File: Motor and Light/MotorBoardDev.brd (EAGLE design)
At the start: 98.5 x 86 mm, 92 parts, among them IC1 74HC04D, J1 Under Glow, J2 Safety Light, J3 12V, J4 24V, Q1 BC846ASMD, Q2 220mA/50V/3.5Ω, Q7 220mA/50V/3.5Ω, Q8 220mA/50V/3.5Ω, Q9 220mA/50V/3.5Ω, T12 TIP41A, T13 TIP41A, T14 TIP41A, T15 TIP41A, T16 TIP41A, T18 TIP41A, T2 TIP41A, U1 TIP41C, U2 9DoF IMU, U3 TIP41C, U4 TIP41C, X1 C-GRID-05-15-91, X2 C-GRID-05-15-91, X4 C-GRID-02-70553, X5 SI-50170, X7 2510-, X8 2510-

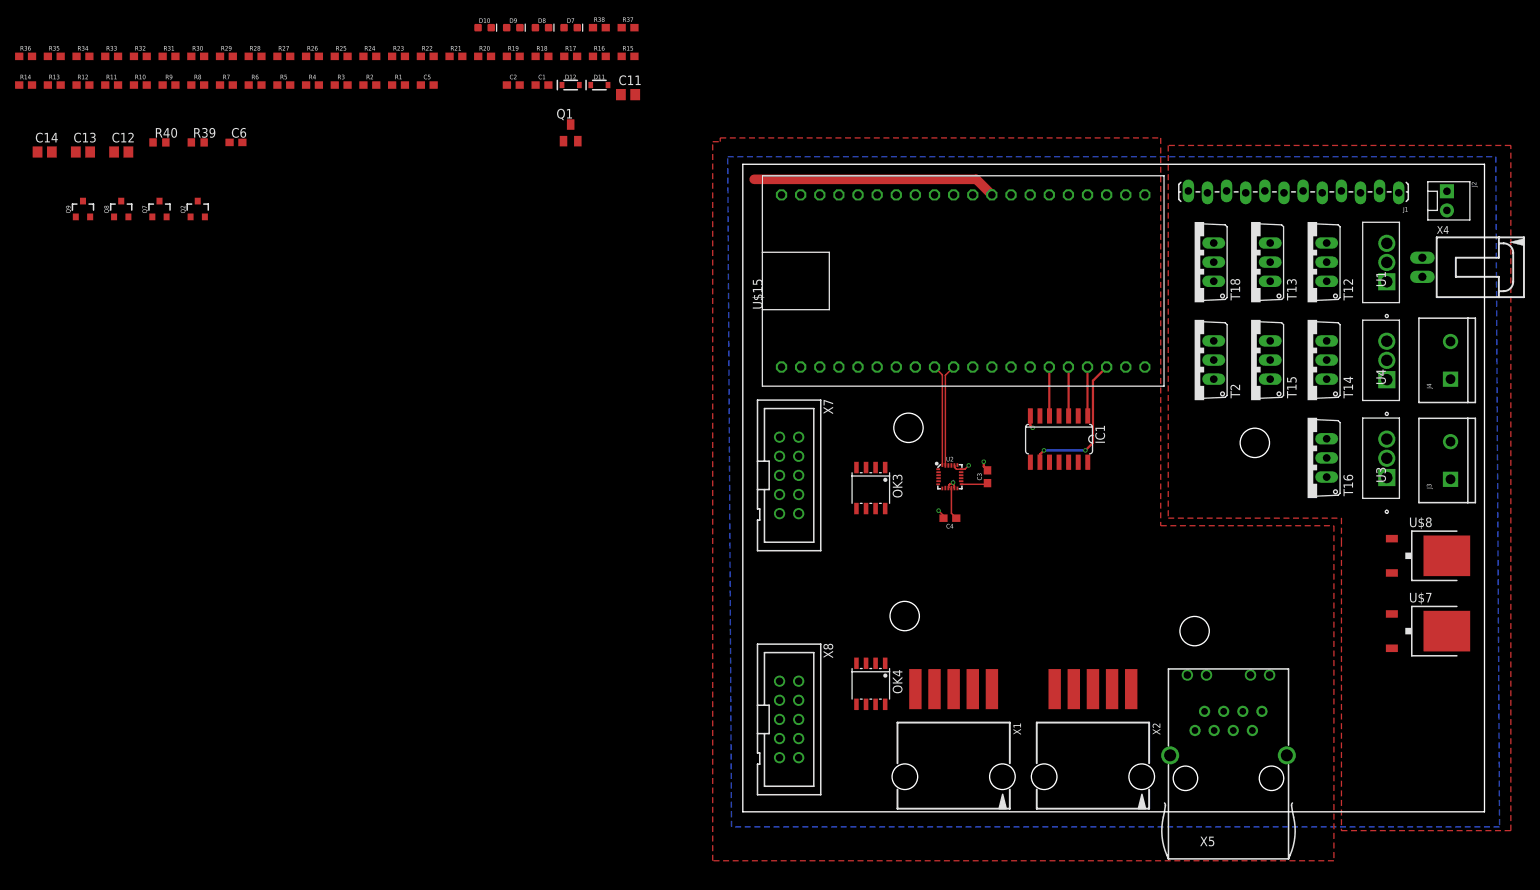
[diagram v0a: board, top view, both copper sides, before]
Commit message: Primary Layout Complete
Layout Complete, Sorting through Libraries
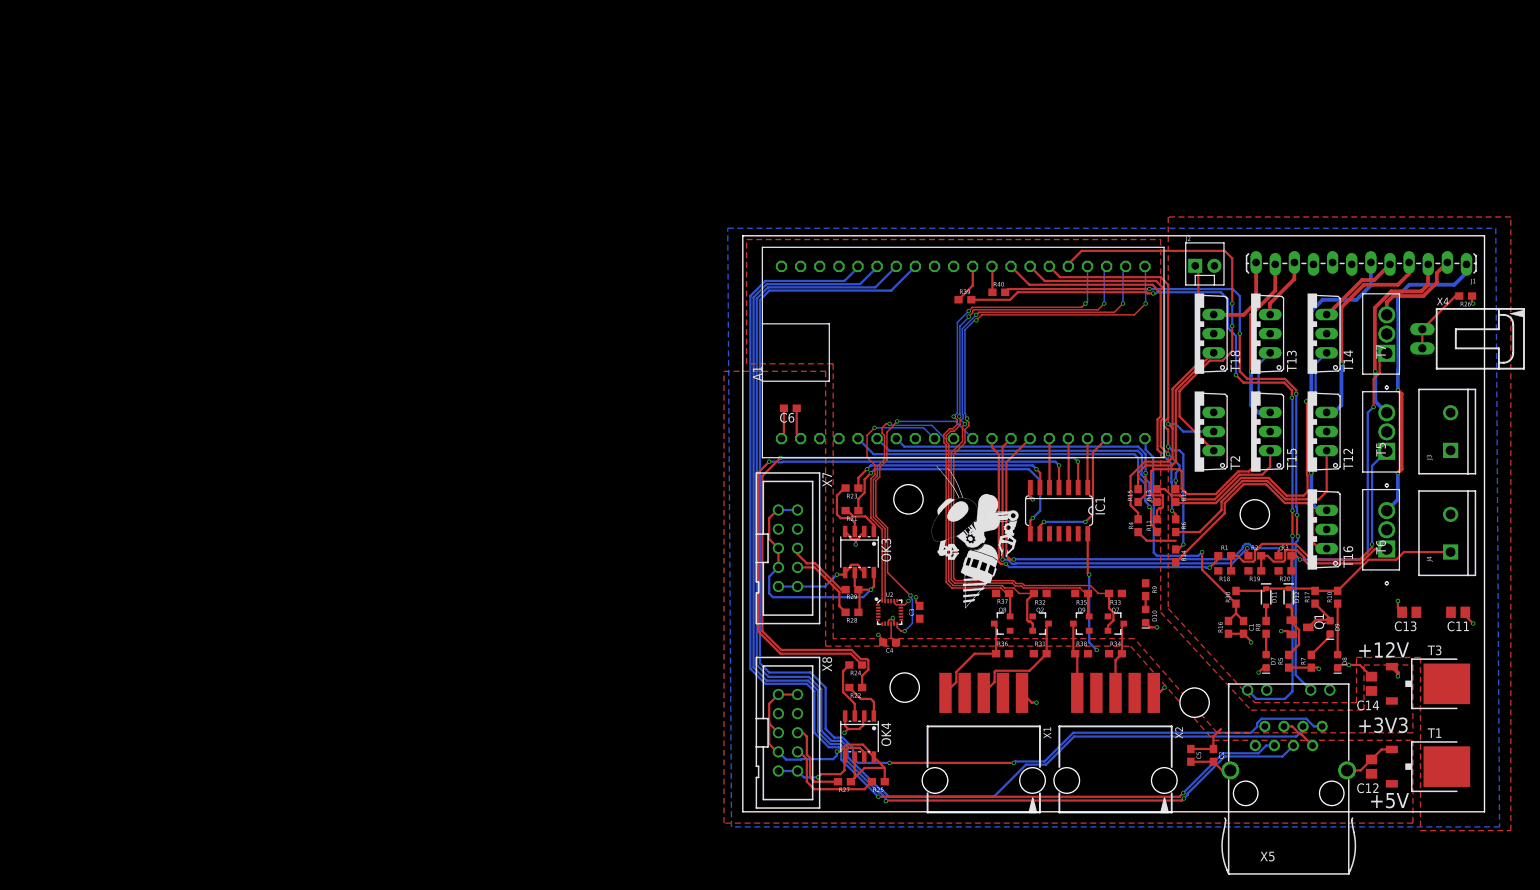
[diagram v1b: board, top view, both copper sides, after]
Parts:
- removed U$15: MBED1768, SparkFun-Boards:DIL40_0.9
- removed U$7: NCP1117DT50GOS-ND, IGVC-Regulators:TO252
- removed U$8: NCP1117DT33GOS-ND, IGVC-Regulators:TO252
- removed U1, U3, U4: TIP41C, DigiKey:TO-220
- added A1: MBED1768, MotorBoardDev:SPARKFUN-BOARDS_DIL40_0.9
- added T1: NCP1117DT50GOS-ND, IGVC-Regulators:TO252
- added T3: NCP1117DT33GOS-ND, IGVC-Regulators:TO252
- added T5, T6, T7: TIP41C, DigiKey:TO-220
- added U$5: (no value), RoboJackets-Aesthetics:ROBOBUZZ_1.0X
- R39, R40: value 150 -> 500; device rcl:R0603 -> SparkFun-Resistors:0603
- moved C14 189.8 mm to (83.5, 17.0), turned to 90 degrees
- moved C13 186.4 mm to (88.5, 26.5), turned to 180 degrees
- moved C12 185.0 mm to (83.5, 6.00), turned to 90 degrees
- moved R10 172.9 mm to (79.0, 28.5), turned to 90 degrees
- moved R14 165.0 mm to (57.5, 34.0), turned to 270 degrees
- moved R7 163.1 mm to (75.5, 20.0), turned to 90 degrees
- moved R8 159.1 mm to (69.5, 24.5), turned to 90 degrees
- moved R34 158.4 mm to (49.5, 21.0), turned to 180 degrees
- moved R26 156.4 mm to (96.0, 68.5), turned to 180 degrees
- moved R13 156.3 mm to (55.0, 42.0), turned to 90 degrees
- moved R30 155.5 mm to (65.5, 28.5), turned to 90 degrees
- moved R12 155.0 mm to (57.5, 42.0), turned to 270 degrees
- moved R35 154.0 mm to (45.0, 29.0), turned to 180 degrees
- moved R5 153.8 mm to (72.5, 20.0), turned to 90 degrees
- moved R36 152.1 mm to (34.5, 21.0)
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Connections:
- net +12V: now also T1.3, T3.3, T5.2, T6.2, T7.2; no longer U$7.3, U$8.3, U1.2, U3.2, U4.2
- net +3V3: now also A1.40, T3.2; no longer U$15.40, U$8.2
- net +5V: now also A1.2, T1.2; no longer U$15.2, U$7.2
- net 1S1: now also A1.28; no longer U$15.28
- net 1S2: now also A1.27; no longer U$15.27
- net 1S3: now also A1.26; no longer U$15.26
- net 2S1: now also A1.5; no longer U$15.5
- net 2S2: now also A1.6; no longer U$15.6
- net 2S3: now also A1.7; no longer U$15.7
- net BATTIN: now also A1.20; no longer U$15.20
- net BLUE: now also A1.13; no longer U$15.12
- net BLUE_OUT: now also T6.3; no longer U3.3
- net GND: now also A1.1, T1.1, T3.1; no longer U$15.1, U$7.1, U$8.1
- net GREEN: now also A1.14; no longer U$15.13
- net GREEN_OUT: now also T7.3; no longer U4.3
- net GYRO_INT: now also A1.11; no longer U$15.14
- net LDIR: now also A1.17; no longer U$15.17
- net LEA3: now also A1.23; no longer U$15.24
- net LEB3: now also A1.24; no longer U$15.23
- net LSPEED: now also A1.18; no longer U$15.18
- net N$10: now also T7.1; no longer U4.1
- net N$3: now also T5.1; no longer U1.1
- net N$37: now also A1.30; no longer U$15.30
- net N$38: now also A1.29; no longer U$15.29
- net N$4: now also T6.1; no longer U3.1
- net RD+: now also A1.35; no longer U$15.35
- net RD-: now also A1.36; no longer U$15.36
- net RDIR: now also A1.15; no longer U$15.15
- net REA3: now also A1.21; no longer U$15.22
- net REB3: now also A1.22; no longer U$15.21
- net RED: now also A1.12; no longer U$15.11
- net RED_OUT: now also T5.3; no longer U1.3
- net RSPEED: now also A1.16; no longer U$15.16
- net SAFETY_LIGHT: now also A1.25; no longer U$15.25
- net SCL: now also A1.10; no longer U$15.10
- net SDA: now also A1.9; no longer U$15.9
- net TD+: now also A1.33; no longer U$15.33
- net TD-: now also A1.34; no longer U$15.34
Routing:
- net TD+: track 0.00 -> 158.0 mm, vias 0 -> 2
- net TD-: track 0.00 -> 156.9 mm
- net RD+: track 0.00 -> 153.9 mm, vias 0 -> 2
- net RD-: track 0.00 -> 149.0 mm, vias 0 -> 2
- net ETH_LED1: track 0.00 -> 100.7 mm, vias 0 -> 5
- net REA3: track 0.00 -> 91.6 mm, vias 0 -> 3
- net ETH_LED2: track 0.00 -> 91.1 mm, vias 0 -> 5
- net !RSPEED!: track 0.00 -> 86.8 mm, vias 0 -> 2
- net REB3: track 0.00 -> 84.4 mm, vias 0 -> 3
- net !RDIR!: track 0.00 -> 80.5 mm, vias 0 -> 2
- net LEA3: track 0.00 -> 78.6 mm, vias 0 -> 3
- net LEB3: track 0.00 -> 71.2 mm, vias 0 -> 3
- net GREEN: track 0.00 -> 56.0 mm, vias 0 -> 2
- net GND: track 8.93 -> 64.5 mm, vias 5 -> 19
- net SAFETY_LIGHT: track 0.00 -> 54.5 mm, vias 0 -> 2
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- added copper zone on layer 1, net +5V
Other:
- board size 98.5 x 86 mm -> 98.5 x 76.5 mm
- board text added: "+12V"
- board text added: "+3V3"
- board text added: "+5V"

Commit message: Updated Schematics Commit
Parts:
- removed D10: WHITE, SparkFun-LED:LED-0603
- removed D11, D12: 3.3V, SparkFun-DiscreteSemi:SOD-323
- removed D7: RED, SparkFun-LED:LED-0603
- removed D8: BLUE, SparkFun-LED:LED-0603
- removed D9: GREEN, SparkFun-LED:LED-0603
- removed IC1: 74HC04D, 74xx-eu:SO14
- removed R18, R19, R20: 200, SparkFun-Resistors:0603
- removed R26, R30: 2700, SparkFun-Resistors:0603
- removed T12, T13, T14, T15, T16, T18: TIP41A, transistor:TO220V
- removed T5, T6, T7: TIP41C, DigiKey:TO-220
- added C7, C8: 10uF, rcl:C0805
- added D1, D2: GREEN, SparkFun-LED:LED-0603
- added D3: WHITE, SparkFun-LED:LED-0603
- added D4: BLUE, SparkFun-LED:LED-0603
- added FQP30N06L, Q15, Q16: TIP41C, transistor-power:TO220AV
- added Q10, Q11, Q3, Q4, Q5, Q6: TIP42C, transistor-power:TO220AV
- added X3: MINI-USB_SHIELD5P4-32005-400, con-cypressindustries:32005-400
- C11, C12, C13, C14: value (none) -> 10uF
- Q1: value BC846ASMD -> TIP42C; device transistor-npn:SOT23 -> transistor-power:TO220AV
- R10: value 2700 -> 200
- R16: value 536 -> 200
- R7: value 200 -> 50
- R8: value 2700 -> 1800
- R9: value 2700 -> 1000
- U$5: device RoboJackets-Aesthetics:ROBOBUZZ_1.0X -> RoboJackets-Aesthetics:ROBOBUZZ_1.2X
- moved R17 348.9 mm to (0.00, -312.0), turned to 0 degrees
- moved C1 324.4 mm to (0.00, -293.0), turned to 0 degrees
- moved R10 324.3 mm to (0.00, -286.0), turned to 0 degrees
- moved R16 320.6 mm to (0.00, -289.5), turned to 0 degrees
- moved R9 316.6 mm to (0.00, -282.5), turned to 0 degrees
- moved R8 311.4 mm to (0.00, -279.0), turned to 0 degrees
- moved R7 298.2 mm to (0.00, -268.5), turned to 0 degrees
- moved R5 294.1 mm to (0.00, -265.0), turned to 0 degrees
- moved Q1 107.5 mm to (7.50, -60.0), turned to 0 degrees
- moved T2 95.3 mm to (7.50, -29.0), turned to 0 degrees
- moved U$5 4.27 mm to (28.0, 23.0)
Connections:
- removed net !LDIR!: IC1.6, R23.1
- removed net !LSPEED!: IC1.8, R21.1
- removed net !RDIR!: IC1.4, R24.1
- removed net !RSPEED!: IC1.2, R22.1
- removed net N$24: D9.A, Q1.3, R17.1
- removed net N$33: D9.C, R7.2
- removed net N$34: D8.A, R10.1
- removed net N$35: D10.A, R9.1
- removed net N$7: D7.A, R8.1
- new net D+: A1.31, X3.3
- new net D-: A1.32, X3.2
- new net ID: X3.4
- new net INDICATOR_LED: A1.8
- new net N$12: D4.A, R9.1
- new net N$5: D1.A, R5.1
- new net N$8: Q11.E, R17.1, X4.1
- net +12V: now also C7.1, FQP30N06L.C, Q15.C, Q16.C, R17.2, R9.2; no longer R18.2, R19.2, R20.2, T5.2, T6.2, T7.2
- net +24V: now also C8.1, R8.2; no longer D11.C, D12.C, R17.2, R30.2
- net +3V3: now also R7.2; no longer R9.2
- net +5V: now also A1.39, R5.2, X3.1; no longer IC1.14
- net 1S1: now also A1.16; no longer A1.28
- net 1S1O: now also J1.7, Q1.E; no longer J1.4, T12.3
- net 1S2: now also A1.17; no longer A1.27
- net 1S2O: now also J1.6, Q4.E; no longer J1.5, T14.3
- net 1S3: now also A1.18; no longer A1.26
- net 1S3O: now also J1.5, Q6.E; no longer J1.6, T16.3
- net 2S1O: now also Q3.E; no longer T13.3
- net 2S2O: now also Q5.E; no longer T15.3
- net 2S3O: now also Q10.E; no longer T18.3
- net BATTIN: now also R10.1; no longer R30.1
- net BLUE: now also A1.21; no longer A1.13
- net BLUE_OUT: now also Q15.E; no longer T6.3
- net ESTOP: now also A1.24, Q11.B; no longer R26.2, X4.1, X4.2
- net GND: now also C7.2, C8.2, D1.C, D2.C, D3.C, D4.C, J1.4, J1.8, J1.9, J2.2, Q1.C, Q10.C, Q11.C, Q3.C, Q4.C, Q5.C, Q6.C, T2.2, X3.5, X4.2; no longer D10.C, D7.C, D8.C, IC1.7, Q1.2, R26.1, R5.1, R7.1, T12.2, T13.2, T14.2, T15.2, T16.2, T18.2, T2.3
- net GREEN: now also A1.22; no longer A1.14
- net GREEN_OUT: now also Q16.E; no longer T7.3
- net L+12V: now also R28.2; no longer OK3.6, OK3.8, R28.1
- net LALI: now also OK3.8
- net LBLI: now also OK3.6, R28.1; no longer R28.2
- net LDIR: now also A1.26, R23.1; no longer A1.17, IC1.1
- net LEA3: now also A1.13; no longer A1.23
- net LEB3: now also A1.12; no longer A1.24
- net LSPEED: now also A1.25, R21.1; no longer A1.18, IC1.9
- net N$1: now also T2.3; no longer T2.2
- net N$10: now also Q16.B; no longer R20.1, T7.1
- net N$11: now also Q6.B; no longer T16.1
- net N$13: now also Q4.B; no longer T14.1
- net N$14: now also Q1.B; no longer T12.1
- net N$15: now also Q3.B; no longer T13.1
- net N$16: now also Q5.B; no longer T15.1
- net N$28: now also Q10.B; no longer T18.1
- net N$3: now also FQP30N06L.B; no longer R18.1, T5.1
- net N$4: now also Q15.B; no longer R19.1, T6.1
- net N$6: now also D2.A, R7.1; no longer D11.A, R8.2
- net N$9: now also D3.A, R8.1; no longer D12.A, Q1.1, R5.2
- net R+12V: now also R25.2, R27.2; no longer OK4.6, OK4.8, R25.1, R27.1
- net RALI: now also OK4.8, R27.1; no longer R27.2
- net RBLI: now also OK4.6, R25.1; no longer R25.2
- net RDIR: now also A1.28, R24.1; no longer A1.15, IC1.5
- net REA3: now also A1.15; no longer A1.21
- net REB3: now also A1.14; no longer A1.22
- net RED: now also A1.23; no longer A1.12
- net RED_OUT: now also FQP30N06L.E; no longer T5.3
- net RSPEED: now also A1.27, R22.1; no longer A1.16, IC1.3
- net SAFETY_LIGHT: now also A1.19; no longer A1.25
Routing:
- net !RSPEED!: track 86.8 -> 0.00 mm, vias 2 -> 0
- net !RDIR!: track 80.5 -> 0.00 mm, vias 2 -> 0
- net RSPEED: track 6.51 -> 83.4 mm, vias 0 -> 2
- net RDIR: track 6.55 -> 77.6 mm, vias 0 -> 2
- net SAFETY_LIGHT: track 54.5 -> 0.00 mm, vias 2 -> 0
- net !LSPEED!: track 36.6 -> 0.00 mm, vias 2 -> 0
- net +24V: track 30.9 -> 0.00 mm
- net 1S3O: track 40.3 -> 11.1 mm, vias 2 -> 0
- net 1S2O: track 11.2 -> 40.3 mm, vias 0 -> 2
- net !LDIR!: track 28.5 -> 0.00 mm, vias 2 -> 0
- net 1S1O: track 27.7 -> 0.00 mm, vias 1 -> 0
- net LDIR: track 6.51 -> 28.5 mm, vias 0 -> 2
- net +5V: track 21.2 -> 5.25 mm, vias 2 -> 0
- net LSPEED: track 19.5 -> 34.9 mm
- net R+12V: track 40.2 -> 27.3 mm
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
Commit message: Layout Initial Commit
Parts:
- removed C7, C8: 10uF, rcl:C0805
- added R18, R19: 4.7k, SparkFun-Resistors:0603
- U$1, U$2, U$3, U$4: device temp:STANDOFF-HOLE -> MotorBoardDev:STANDOFF-HOLE
- U$5: device RoboJackets-Aesthetics:ROBOBUZZ_1.2X -> MotorBoardDev:ROBOBUZZ_1.2X
- moved R9 346.7 mm to (11.0, 64.0), turned to 90 degrees
- moved R7 346.0 mm to (19.5, 77.0), turned to 90 degrees
- moved D2 335.6 mm to (19.5, 73.5), turned to 270 degrees
- moved D4 335.2 mm to (11.0, 59.5), turned to 270 degrees
- moved R17 334.7 mm to (12.0, 22.5), turned to 90 degrees
- moved C1 309.3 mm to (33.0, 14.5)
- moved R16 303.8 mm to (33.0, 12.5), turned to 180 degrees
- moved R10 299.9 mm to (29.0, 12.5), turned to 180 degrees
- moved R8 293.2 mm to (12.0, 14.0), turned to 270 degrees
- moved D3 290.3 mm to (12.0, 18.0), turned to 90 degrees
- moved FQP30N06L 279.0 mm to (8.50, 33.0), turned to 90 degrees
- moved R5 272.5 mm to (17.0, 7.00), turned to 90 degrees
- moved Q16 263.6 mm to (15.0, 33.0), turned to 90 degrees
- moved D1 261.7 mm to (17.0, 3.10), turned to 270 degrees
- moved Q15 248.6 mm to (21.6, 33.2), turned to 90 degrees
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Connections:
- net +12V: no longer C7.1
- net +24V: no longer C8.1
- net +3V3: now also R18.2, R19.2
- net 1S1: now also A1.18; no longer A1.16
- net 1S3: now also A1.16; no longer A1.18
- net 2S1: now also A1.7; no longer A1.5
- net 2S3: now also A1.5; no longer A1.7
- net GND: no longer C7.2, C8.2
- net LEA3: now also A1.14; no longer A1.13
- net LEB3: now also A1.15; no longer A1.12
- net REA3: now also A1.12; no longer A1.15
- net REB3: now also A1.13; no longer A1.14
- net SCL: now also R18.1
- net SDA: now also R19.1
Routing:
- net TD-: track 156.9 -> 22.0 mm, vias 0 -> 1
- net RD+: track 153.9 -> 20.7 mm, vias 2 -> 1
- net TD+: track 158.0 -> 25.8 mm, vias 2 -> 0
- net RD-: track 149.0 -> 21.5 mm, vias 2 -> 0
- net ETH_LED1: track 100.7 -> 12.9 mm, vias 5 -> 0
- net ESTOP: track 0.00 -> 70.9 mm, vias 0 -> 5
- net D-: track 0.00 -> 70.9 mm, vias 0 -> 1
- net D+: track 0.00 -> 69.8 mm, vias 0 -> 3
- net ETH_LED2: track 91.1 -> 23.8 mm, vias 5 -> 0
- net REA3: track 91.5 -> 36.2 mm, vias 3 -> 2
- net +3V3: track 10.9 -> 57.9 mm, vias 0 -> 5
- net REB3: track 83.9 -> 38.6 mm, vias 3 -> 2
- net 1S3: track 52.4 -> 15.8 mm, vias 2 -> 1
- net RSPEED: track 83.4 -> 48.7 mm, vias 2 -> 1
- net LEA3: track 78.2 -> 44.8 mm, vias 3 -> 2
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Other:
- board size 98.5 x 76.5 mm -> 93.5 x 80.5 mm
- board text removed: "+12V"
- board text removed: "+3V3"
- board text removed: "+5V"

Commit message: Before Review
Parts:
- moved X5 0.81 mm to (86.8, 68.1)
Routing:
- net TD+: track 25.8 -> 22.2 mm, vias 0 -> 1
- net D+: track 69.8 -> 73.0 mm
- net ETH_LED2: track 23.8 -> 26.3 mm, vias 0 -> 2
- net TD-: track 22.0 -> 20.1 mm, vias 1 -> 0
- net ETH_LED1: track 12.9 -> 13.7 mm
- net RD-: track 21.5 -> 21.1 mm, vias 0 -> 2

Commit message: Somehoe the branch still exists
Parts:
- added D5: BLUE, SparkFun-LED:LED-0603
- added U1: TXB0104DR, MotorBoardDev:D14
- D3: value WHITE -> Yellow
- R10: value 200 -> 4.7k
- R16: value 200 -> 500
- R25, R27, R28, R29: value 10k -> 4.7k
- moved D3 0.25 mm to (12.0, 17.8)
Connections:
- net D+ renamed D_P
- net D- renamed D_N
- net RD+ renamed RD_P
- net RD- renamed RD_N
- net TD+ renamed TD_P
- net TD- renamed TD_N
- removed net ID: X3.4
- new net N$7: J2.2, T2.3
- new net VCCA: U1.1
- new net VCCB: U1.14
- net BLUE: no longer A1.21
- net ESTOP: now also A1.22; no longer A1.24
- net GND: now also D5.C, U1.7; no longer J1.4, J1.8, J1.9, J2.2
- net GREEN: no longer A1.22
- net INDICATOR_LED: now also D5.A
- net LDIR: now also A1.24; no longer A1.26
- net LSPEED: now also A1.23; no longer A1.25
- net N$1: no longer T2.3
- net RDIR: now also A1.26; no longer A1.28
- net RED: no longer A1.23
- net RSPEED: now also A1.25; no longer A1.27
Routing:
- net RD_N: track 21.1 -> 9.40 mm
- net RD_P: track 21.1 -> 9.44 mm
- net TD_N: track 20.1 -> 11.1 mm
- net RDIR: track 55.8 -> 51.0 mm
- net N$1: track 32.3 -> 28.9 mm
- net LSPEED: track 27.4 -> 24.7 mm
- net RED: track 60.6 -> 58.0 mm
- net ESTOP: track 70.9 -> 69.0 mm
- net BLUE: track 43.3 -> 41.9 mm
